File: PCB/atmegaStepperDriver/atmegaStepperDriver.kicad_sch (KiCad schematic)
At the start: 54 parts, among them J1 General power, J2 Motor Output, J3 Motor power, J4 FanSocket, J5 Reset Header, J6 I2C Communication pins, J8 Programming socket 01x06, J9 Stepper communication pins, Q13 BC547, Q17 BC547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

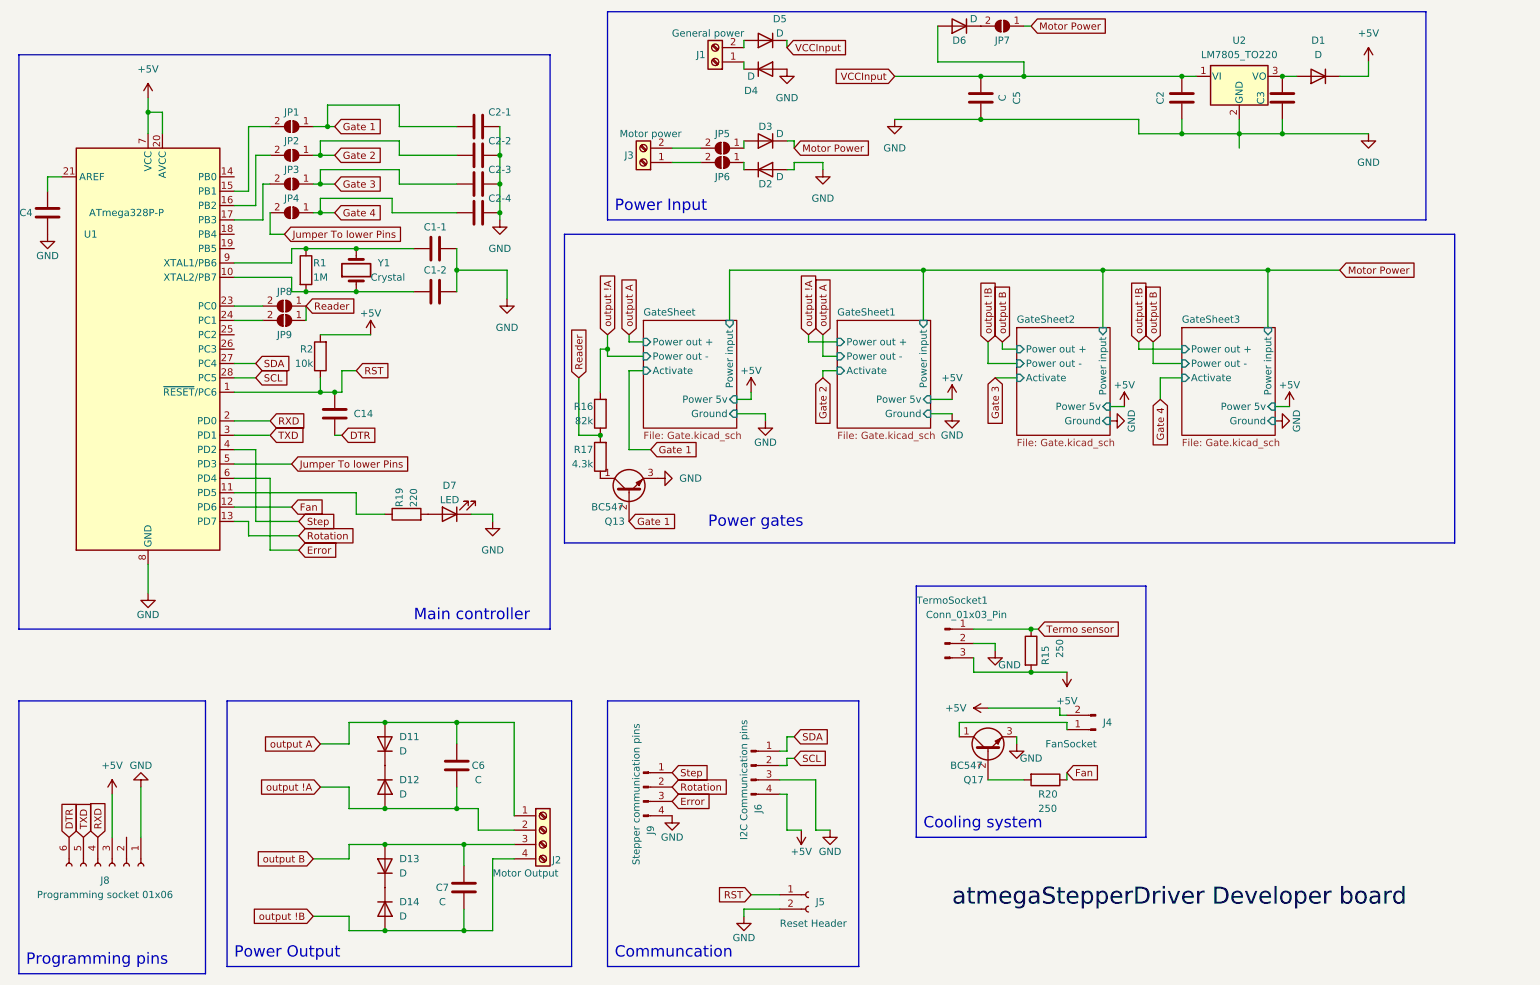
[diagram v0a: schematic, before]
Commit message: Added analog read for motor error
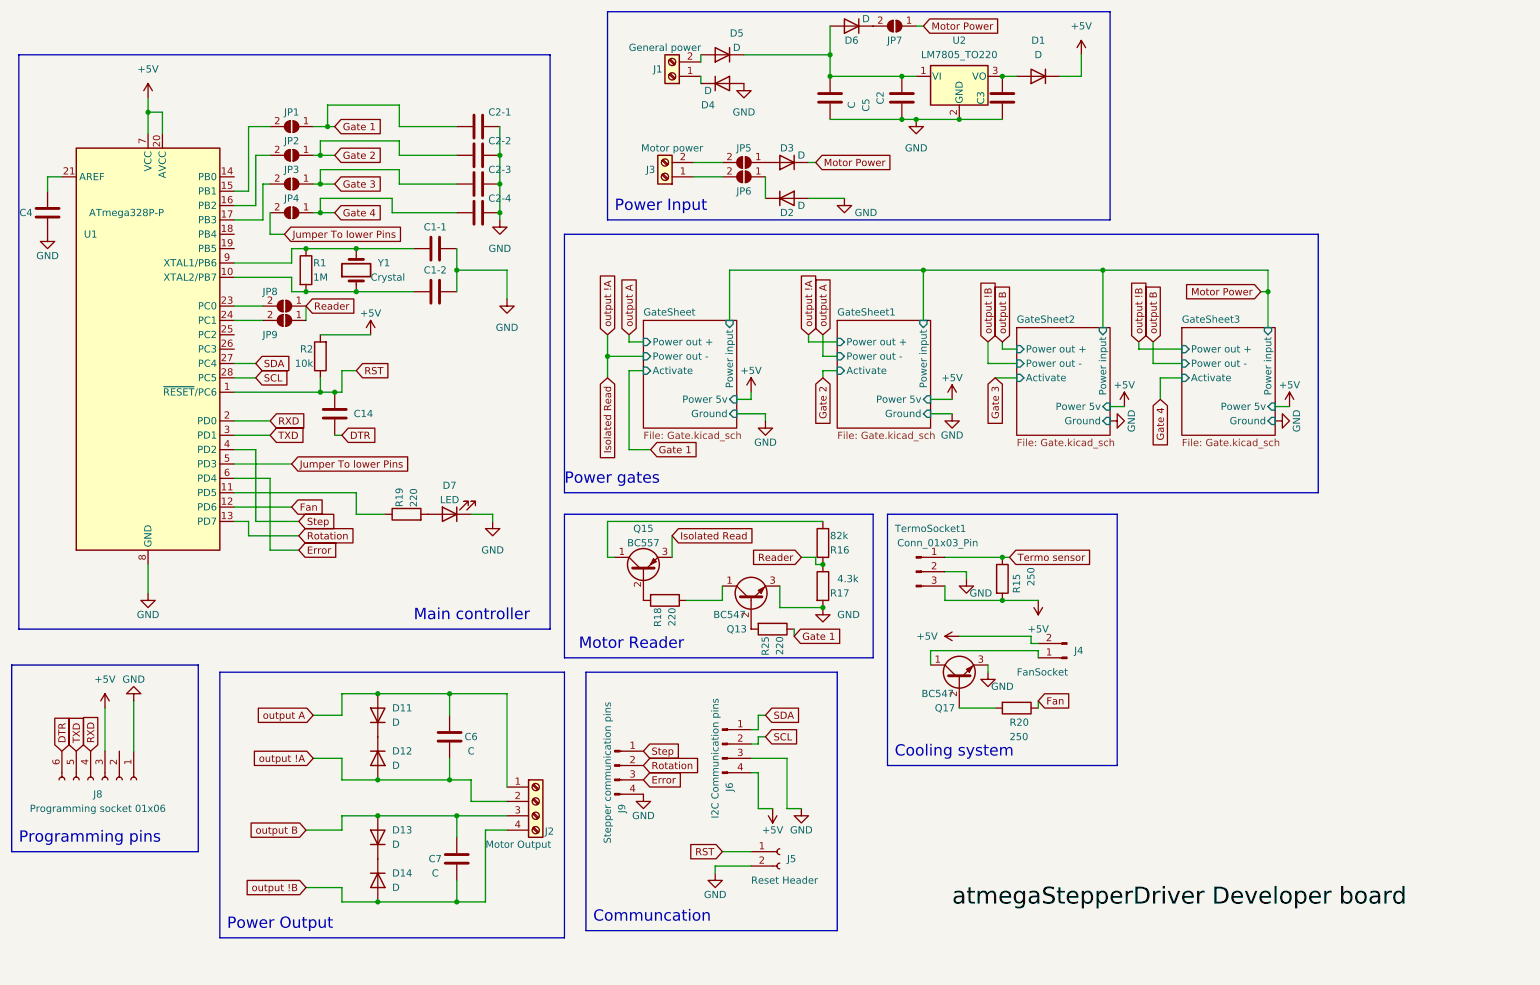
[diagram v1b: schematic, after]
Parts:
- added Q15: BC557, Package_TO_SOT_THT:TO-92_Inline_Wide, symbol Transistor_BJT:BC557
- added R18, R25: 220, Resistor_THT:R_Axial_DIN0207_L6.3mm_D2.5mm_P10.16mm_Horizontal, symbol Device:R
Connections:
- net GND: now also R17.2
- net Gate 1: now also R25.1; no longer Q13.2 (B)
- net Reader: now also R16.2, R17.1; no longer R16.1, R17.2
- net at Q13.1 (C): now also R18.1; no longer R17.1
- net VCCInput: no longer names the net of C2.2, C5.1, D5.1 (K), D6.2 (A), U2.1 (VI)
- net output !A renamed Isolated Read
- net Isolated Read: now also Q15.3 (E); no longer R16.2
- new net: Q15.1 (C), R16.1
- new net: Q15.2 (B), R18.2
- new net: Q13.2 (B), R25.2
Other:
- note added: "Motor Reader"
- moved on the sheet: C2, C3, C5, C6, C7, D1, D11, D12, D13, D14, D2, D3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

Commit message: someData; idk what i did, forgot to push it
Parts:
- added AP_JP1, MP_JP1: SolderJumper_2_Open, Jumper:SolderJumper-2_P1.3mm_Open_RoundedPad1.0x1.5mm, symbol Jumper:SolderJumper_2_Open
- added C1: C, Capacitor_THT:CP_Radial_D8.0mm_P3.80mm, symbol Device:C
- added GND_R1: 250, Resistor_THT:R_Axial_DIN0207_L6.3mm_D2.5mm_P10.16mm_Horizontal, symbol Device:R
- Q15: footprint Package_TO_SOT_THT:TO-92_Inline_Wide -> Package_TO_SOT_THT:TO-92_Inline
- renumbered R15 to 5V_R1, J4 to FanSocket1, JP7 to M_JP1, D6 to m_D1
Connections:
- net +5V: now also AP_JP1.1 (A)
- net GND: now also C1.2, GND_R1.2
- net Gate 1: no longer R25.1
- net Motor Power: now also C1.1, MP_JP1.1 (A)
- net Termo sensor: now also GND_R1.1
- net activeRead: now reaches U1.18 (PB4)
- net activeRead: now also R25.1
- new net GateSheet/Power 5v: AP_JP1.2 (B), MP_JP1.2 (B)
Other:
- moved on the sheet: 5V_R1, C1-1, C1-2, R1, Y1
